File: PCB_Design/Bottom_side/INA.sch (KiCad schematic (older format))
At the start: 4 parts

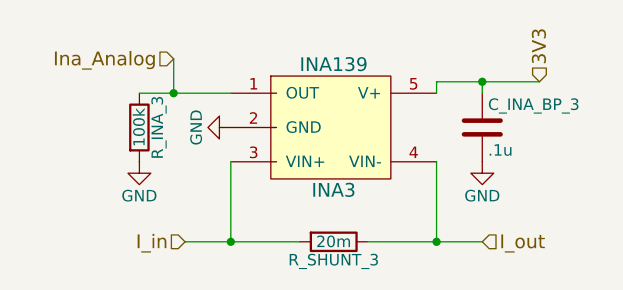
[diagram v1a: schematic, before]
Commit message: Updated PCB structure tree
Full_PCB now includes bottom and top layer hierarchical sheets
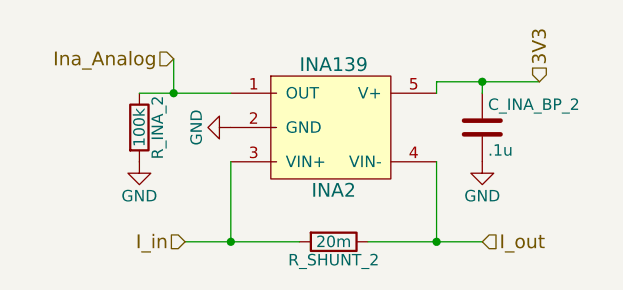
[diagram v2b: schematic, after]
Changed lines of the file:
@@
 LIBS:power
 LIBS:device
-LIBS:switches
-LIBS:relays
-LIBS:motors
 LIBS:transistors
 LIBS:conn
@@
 LIBS:contrib
 LIBS:valves
-LIBS:Bottom_side-cache
+LIBS:Full_PCB-cache
 EELAYER 25 0
 EELAYER END
@@
 AR Path="/5A57B48D/5A57B575/5A681ED4/5A57C277" Ref="#PWR08"  Part="1"
 AR Path="/5A57B48D/5A57B575/5A6821BC/5A57C277" Ref="#PWR011"  Part="1"
-F 0 "#PWR011" H 2500 1650 50  0001 C CNN
+F 0 "#PWR08" H 2500 1650 50  0001 C CNN
 F 1 "GND" H 2500 1750 50  0000 C CNN
 F 2 "" H 2500 1900 50  0001 C CNN
@@
 AR Path="/5A57B48D/5A57B575/5A681ED4/5A57C067" Ref="INA2"  Part="1"
 AR Path="/5A57B48D/5A57B575/5A6821BC/5A57C067" Ref="INA3"  Part="1"
-F 0 "INA3" H 3350 1475 60  0000 C CNN
+F 0 "INA2" H 3350 1475 60  0000 C CNN
 F 1 "INA139" H 3350 2025 60  0000 C CNN
 F 2 "TO_SOT_Packages_SMD:SOT-23-5" H 3225 1800 60  0001 C CNN
@@
 AR Path="/5A57B48D/5A57B575/5A681ED4/5A57BEEA" Ref="#PWR09"  Part="1"
 AR Path="/5A57B48D/5A57B575/5A6821BC/5A57BEEA" Ref="#PWR012"  Part="1"
-F 0 "#PWR012" H 2900 1500 50  0001 C CNN
+F 0 "#PWR09" H 2900 1500 50  0001 C CNN
 F 1 "GND" H 2900 1600 50  0000 C CNN
 F 2 "" H 2900 1750 50  0001 C CNN
@@
 AR Path="/5A57B48D/5A57B575/5A681ED4/5A57BEBA" Ref="#PWR010"  Part="1"
 AR Path="/5A57B48D/5A57B575/5A6821BC/5A57BEBA" Ref="#PWR013"  Part="1"
-F 0 "#PWR013" H 4000 1650 50  0001 C CNN
+F 0 "#PWR010" H 4000 1650 50  0001 C CNN
 F 1 "GND" H 4000 1750 50  0000 C CNN
 F 2 "" H 4000 1900 50  0001 C CNN
@@
 AR Path="/5A57B48D/5A57B575/5A681ED4/5A57BCFE" Ref="C_INA_BP_2"  Part="1"
 AR Path="/5A57B48D/5A57B575/5A6821BC/5A57BCFE" Ref="C_INA_BP_3"  Part="1"
-F 0 "C_INA_BP_3" H 4025 1850 50  0000 L CNN
+F 0 "C_INA_BP_2" H 4025 1850 50  0000 L CNN
 F 1 ".1u" H 4025 1650 50  0000 L CNN
 F 2 "Capacitors_SMD:C_0603" H 4038 1600 50  0001 C CNN
@@
 AR Path="/5A57B48D/5A57B575/5A681ED4/5A57BCC0" Ref="R_SHUNT_2"  Part="1"
 AR Path="/5A57B48D/5A57B575/5A6821BC/5A57BCC0" Ref="R_SHUNT_3"  Part="1"
-F 0 "R_SHUNT_3" V 3430 2250 50  0000 C CNN
+F 0 "R_SHUNT_2" V 3430 2250 50  0000 C CNN
 F 1 "20m" V 3350 2250 50  0000 C CNN
 F 2 "Resistors_SMD:R_0805" V 3280 2250 50  0001 C CNN
@@
 AR Path="/5A57B48D/5A57B575/5A681ED4/5A57BC8F" Ref="R_INA_2"  Part="1"
 AR Path="/5A57B48D/5A57B575/5A6821BC/5A57BC8F" Ref="R_INA_3"  Part="1"
-F 0 "R_INA_3" V 2580 1750 50  0000 C CNN
+F 0 "R_INA_2" V 2580 1750 50  0000 C CNN
 F 1 "100k" V 2500 1750 50  0000 C CNN
 F 2 "Resistors_SMD:R_0603" V 2430 1750 50  0001 C CNN
